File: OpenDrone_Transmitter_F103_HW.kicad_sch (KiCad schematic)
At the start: 75 parts, among them J1 Conn_01x03, J10 Conn_01x04, J11 Conn_01x03, J12 Conn_01x04, J13 Conn_01x02, J14 Conn_01x05, J15 Conn_01x02, J16 Conn_02x04_Odd_Even, J17 Conn_01x02, J18 Conn_01x02, J19 Conn_01x03, J2 Conn_01x05, J20 Conn_01x02, J21 Conn_01x02, J22 Conn_01x02, J3 Conn_01x03, J4 Conn_01x03, J5 Conn_01x03, J6 Conn_01x02, J7 Conn_01x02, J8 Conn_01x03, J9 Conn_01x03, SW1 RESET, U1 STM32F103C8Tx, U2 AMS1117-3.3, U3 TPS54331, Y2 Crystal_GND24

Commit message: update project
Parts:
- added D4: SS24, Diode_SMD:D_SMA, symbol Device:D_Small
- J10, J12: footprint Footprint:Connector_XH_1x04_P1.25mm_Horizontal -> Footprint:Connector_XH_1x04_P1.25mm_Vertical
- J14, J2: footprint Footprint:Connector_XH_1x05_P1.25mm_Horizontal -> Footprint:Connector_XH_1x05_P1.25mm_Vertical
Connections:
- net GND: now also D4.2 (A)
- net VBAT: now also D4.1 (K)
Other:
- moved on the sheet: C1, C11, C12, C13, C14, C2, C20, C4, C5, D1, D2, D3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

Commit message: update project
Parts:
- R1: value TBD -> 10k
- R2: value TBD -> 3,3k
- R6: value TBD -> 0R
- U3: footprint Package_SO:SOIC-8-1EP_3.9x4.9mm_P1.27mm_EP2.29x3mm_ThermalVias -> Package_SO:SOIC-8-1EP_3.9x4.9mm_P1.27mm_EP2.29x3mm
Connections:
- net +3V3: now also J3.1 (Pin_1)
- net GND: now also J3.3 (Pin_3)
- net LEFT_JOYSTICK_IN1: now also J3.2 (Pin_2)
- net at R2.1, R6.2: now also U3.5 (VSENSE)
- net at R1.2, R6.1: no longer U3.5 (VSENSE)
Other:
- moved on the sheet: R6
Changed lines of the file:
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@@
 	)
 	(junction
+		(at 110.49 184.15)
+		(diameter 0)
+		(color 0 0 0 0)
+	)
+	(junction
 		(at 110.49 190.5)
 		(diameter 0)
@@
 	)
 	(junction
-		(at 110.49 180.34)
-		(diameter 0)
-		(color 0 0 0 0)
-	)
-	(junction
 		(at 38.1 172.72)
 		(diameter 0)
@@
 	(wire
 		(pts
+			(xy 82.55 180.34) (xy 105.41 180.34)
+		)
+		(stroke
+			(width 0)
+			(type default)
+		)
+	)
+	(wire
+		(pts
 			(xy 127 180.34) (xy 127 190.5)
 		)
@@
 	(wire
 		(pts
-			(xy 110.49 180.34) (xy 110.49 179.07)
-		)
-		(stroke
-			(width 0)
-			(type default)
-		)
-	)
-	(wire
-		(pts
 			(xy 138.43 34.29) (xy 143.51 34.29)
 		)
@@
 	(wire
 		(pts
-			(xy 82.55 180.34) (xy 110.49 180.34)
+			(xy 105.41 184.15) (xy 110.49 184.15)
 		)
 		(stroke
@@
 	(wire
 		(pts
+			(xy 110.49 184.15) (xy 110.49 185.42)
+		)
+		(stroke
+			(width 0)
+			(type default)
+		)
+	)
+	(wire
+		(pts
 			(xy 113.03 104.14) (xy 124.46 104.14)
 		)
@@
 	(wire
 		(pts
+			(xy 105.41 180.34) (xy 105.41 184.15)
+		)
+		(stroke
+			(width 0)
+			(type default)
+		)
+	)
+	(wire
+		(pts
 			(xy 133.35 170.18) (xy 135.89 170.18)
 		)
@@
 	(global_label "LEFT_JOYSTICK_IN1"
 		(shape input)
-		(at 189.23 31.75 0)
+		(at 190.5 31.75 0)
 		(fields_autoplaced yes)
 		(effects
@@
 		)
 		(property "Intersheetrefs" "${INTERSHEET_REFS}"
-			(at 210.2371 31.75 0)
+			(at 211.5071 31.75 0)
 			(effects
 				(font
@@
 			)
 		)
-		(property "Value" "TBD"
+		(property "Value" "3,3k"
 			(at 112.268 188.722 0)
 			(effects
@@
 			)
 		)
-		(property "Footprint" "Package_SO:SOIC-8-1EP_3.9x4.9mm_P1.27mm_EP2.29x3mm_ThermalVias"
+		(property "Footprint" "Package_SO:SOIC-8-1EP_3.9x4.9mm_P1.27mm_EP2.29x3mm"
 			(at 69.85 177.8 0)
 			(effects
@@
 	(symbol
 		(lib_id "power:GND")
-		(at 189.23 34.29 90)
+		(at 190.5 34.29 90)
 		(unit 1)
 		(exclude_from_sim no)
@@
 		(fields_autoplaced yes)
 		(property "Reference" "#PWR025"
-			(at 195.58 34.29 0)
+			(at 196.85 34.29 0)
 			(effects
 				(font
@@
 		)
 		(property "Value" "GND"
-			(at 193.04 34.2899 90)
+			(at 194.31 34.2899 90)
 			(effects
 				(font
@@
 		)
 		(property "Footprint" ""
-			(at 189.23 34.29 0)
+			(at 190.5 34.29 0)
 			(effects
 				(font
@@
 		)
 		(property "Datasheet" ""
-			(at 189.23 34.29 0)
+			(at 190.5 34.29 0)
 			(effects
 				(font
@@
 		)
 		(property "Description" "Power symbol creates a global label with name \"GND\" , ground"
-			(at 189.23 34.29 0)
+			(at 190.5 34.29 0)
 			(effects
 				(font
@@
 	(symbol
 		(lib_id "power:+3V3")
-		(at 189.23 29.21 270)
+		(at 190.5 29.21 270)
 		(unit 1)
 		(exclude_from_sim no)
@@
 		(fields_autoplaced yes)
 		(property "Reference" "#PWR026"
-			(at 185.42 29.21 0)
+			(at 186.69 29.21 0)
 			(effects
 				(font
@@
 		)
 		(property "Value" "+3V3"
-			(at 193.04 29.2099 90)
+			(at 194.31 29.2099 90)
 			(effects
 				(font
@@
 		)
 		(property "Footprint" ""
-			(at 189.23 29.21 0)
+			(at 190.5 29.21 0)
 			(effects
 				(font
@@
 		)
 		(property "Datasheet" ""
-			(at 189.23 29.21 0)
+			(at 190.5 29.21 0)
 			(effects
 				(font
@@
 		)
 		(property "Description" "Power symbol creates a global label with name \"+3V3\""
-			(at 189.23 29.21 0)
+			(at 190.5 29.21 0)
 			(effects
 				(font
@@
 			)
 		)
-		(property "Value" "TBD"
+		(property "Value" "10k"
 			(at 112.268 177.8 0)
 			(effects
@@
 	(symbol
 		(lib_id "Device:R_Small")
-		(at 110.49 182.88 0)
+		(at 110.49 181.61 0)
 		(unit 1)
 		(exclude_from_sim no)
@@
 		(dnp no)
 		(property "Reference" "R6"
-			(at 112.268 181.61 0)
+			(at 112.268 180.34 0)
 			(effects
 				(font
@@
 			)
 		)
-		(property "Value" "TBD"
-			(at 112.268 183.642 0)
+		(property "Value" "0R"
+			(at 112.268 182.372 0)
 			(effects
 				(font
@@
 		)
 		(property "Footprint" "Resistor_SMD:R_0603_1608Metric"
-			(at 110.49 182.88 0)
+			(at 110.49 181.61 0)
 			(effects
 				(font
@@
 		)
 		(property "Datasheet" "~"
-			(at 110.49 182.88 0)
+			(at 110.49 181.61 0)
 			(effects
 				(font
@@
 		)
 		(property "Description" "Resistor, small symbol"
-			(at 110.49 182.88 0)
+			(at 110.49 181.61 0)
 			(effects
 				(font

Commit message: complete v1.0
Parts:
- added D5: D_Small, LED_SMD:LED_0603_1608Metric, symbol Device:D_Small
- added R17: 330R, Resistor_SMD:R_0603_1608Metric, symbol Device:R_Small
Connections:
- net +3V3: now also J16.1 (Pin_1), R17.2; no longer J16.2 (Pin_2)
- net BUTTON1: now also J14.4 (Pin_4), U1.30 (PA9); no longer J14.1 (Pin_1), U1.22 (PB11)
- net BUTTON2: now also J14.3 (Pin_3); no longer J14.2 (Pin_2)
- net BUTTON3: now also J14.2 (Pin_2); no longer J14.3 (Pin_3)
- net BUTTON4: now also J14.1 (Pin_1); no longer J14.4 (Pin_4)
- net GND: now also J16.2 (Pin_2), D5.1 (K); no longer J16.1 (Pin_1)
- net NRF24_CE: now also J16.4 (Pin_4); no longer J16.3 (Pin_3)
- net NRF24_CLK: now also J16.6 (Pin_6); no longer J16.5 (Pin_5)
- net NRF24_CS: now also J16.3 (Pin_3); no longer J16.4 (Pin_4)
- net NRF24_IRQ: now also J16.7 (Pin_7), U1.22 (PB11); no longer J16.8 (Pin_8), U1.30 (PA9)
- net NRF24_MISO: now also J16.8 (Pin_8); no longer J16.7 (Pin_7)
- net NRF24_MOSI: now also J16.5 (Pin_5); no longer J16.6 (Pin_6)
- net STM32_CLK: now also J2.4 (Pin_4); no longer J2.3 (Pin_3)
- net STM32_DIO: now also J2.3 (Pin_3); no longer J2.4 (Pin_4)
- net ADC_RESERVED: no longer names the net of U1.19 (PB1)
- new net: D5.2 (A), R17.1
- no-connect marks 1 -> 9
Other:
- moved on the sheet: C15, C27, C28, C29, J12, J13, J15, J17, J18, J20, J21, J22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

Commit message: update
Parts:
- added C10, C21, C30, C31: 100nF, KiCad-Lib:C_0603_1608Metric, symbol Device:C_Small
- added J23: Conn_01x08, KiCad-Lib:Connector_ZH_1x08_P1.25mm_Vertical, symbol Connector_Generic:Conn_01x08
- added R18, R19, R20, R21: 1k, KiCad-Lib:R_0603_1608Metric, symbol Device:R_Small
- C1, C2, C20, C4, C5, C9: footprint Capacitor_SMD:C_1210_3225Metric -> KiCad-Lib:C_1210_3225Metric
- C11, C12, C13, C14, C15, C16, C17, C18, C19, C22, C23, C24, C25, C26, C27, C28, C29, C3, C6, C7, C8: footprint Capacitor_SMD:C_0603_1608Metric -> KiCad-Lib:C_0603_1608Metric
- D1, D2, D3, D4: footprint Diode_SMD:D_SMA -> KiCad-Lib:D_SMA
- D5: footprint LED_SMD:LED_0603_1608Metric -> KiCad-Lib:LED_0603_1608Metric
- J1, J11, J19, J3, J4, J5, J8, J9: footprint Footprint:Connector_XH_1x03_P1.25mm_Vertical -> KiCad-Lib:Connector_ZH_1x03_P1.25mm_Vertical
- J10, J12: footprint Footprint:Connector_XH_1x04_P1.25mm_Vertical -> KiCad-Lib:Connector_ZH_1x04_P1.25mm_Vertical
- J13, J15, J17, J18, J20, J21, J22, J6: footprint Footprint:Connector_XH_1x02_P1.25mm_Vertical -> KiCad-Lib:Connector_ZH_1x02_P1.25mm_Vertical
- J14, J2: footprint Footprint:Connector_XH_1x05_P1.25mm_Vertical -> KiCad-Lib:Connector_ZH_1x05_P1.25mm_Vertical
- J7: footprint Connector_JST:JST_EH_B2B-EH-A_1x02_P2.50mm_Vertical -> KiCad-Lib:Connector_ZH_1x02_P1.25mm_Vertical
- L1: footprint Footprint:Inductor_SMD_4D28 -> KiCad-Lib:Inductor_SMD_4D28
- R1, R10, R11, R12, R13, R14, R15, R16, R17, R2, R3, R4, R5, R6, R7, R8, R9: footprint Resistor_SMD:R_0603_1608Metric -> KiCad-Lib:R_0603_1608Metric
- SW1: footprint Footprint:Button_SMD_4.2x3.3x2.5mm -> KiCad-Lib:Button_SMD_4.2x3.3x2.5mm
- U3: footprint Package_SO:SOIC-8-1EP_3.9x4.9mm_P1.27mm_EP2.29x3mm -> KiCad-Lib:SOIC-8-1EP_3.9x4.9mm_P1.27mm_EP2.29x3mm
- U4: footprint Footprint:Board -> Proj-Lib:Board
- Y2: footprint Crystal:Crystal_SMD_3225-4Pin_3.2x2.5mm -> KiCad-Lib:Crystal_SMD_3225-4Pin_3.2x2.5mm
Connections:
- net +3V3: now also J23.8 (Pin_8), R18.1, R19.1, R20.1, R21.1
- net BUTTON1: now also J14.1 (Pin_1); no longer J14.4 (Pin_4)
- net BUTTON2: now also J14.2 (Pin_2); no longer J14.3 (Pin_3)
- net BUTTON3: now also J14.3 (Pin_3); no longer J14.2 (Pin_2)
- net BUTTON4: now also J14.4 (Pin_4); no longer J14.1 (Pin_1)
- net GND: now also J1.2 (Pin_2), J11.2 (Pin_2), J19.2 (Pin_2), J20.2 (Pin_2), J21.2 (Pin_2), J22.2 (Pin_2), J3.2 (Pin_2), J4.2 (Pin_2), J5.2 (Pin_2), J6.2 (Pin_2), J8.2 (Pin_2), J9.2 (Pin_2), C10.2, C21.2, C30.2, C31.2, J23.7 (Pin_7); no longer J1.3 (Pin_3), J11.3 (Pin_3), J19.3 (Pin_3), J3.3 (Pin_3), J4.3 (Pin_3), J5.3 (Pin_3), J8.3 (Pin_3), J9.3 (Pin_3)
- net I2C1_SCL: now also J10.3 (Pin_3); no longer J10.4 (Pin_4)
- net I2C1_SDA: now also J10.4 (Pin_4); no longer J10.3 (Pin_3)
- net LEFT_JOYSTICK_IN1: now also J3.3 (Pin_3); no longer J3.2 (Pin_2)
- net LEFT_JOYSTICK_IN2: now also J4.3 (Pin_3); no longer J4.2 (Pin_2)
- net NRF24_CE: now also J23.5 (Pin_5)
- net NRF24_CLK: now also J23.3 (Pin_3)
- net NRF24_CS: now also U1.22 (PB11), J23.6 (Pin_6); no longer U1.25 (PB12)
- net NRF24_IRQ: now also U1.38 (PA15), J23.2 (Pin_2); no longer U1.22 (PB11)
- net NRF24_MISO: now also J23.1 (Pin_1)
- net NRF24_MOSI: now also J23.4 (Pin_4)
- net RIGHT_JOYSTICK_IN1: now also J19.3 (Pin_3); no longer J19.2 (Pin_2)
- net RIGHT_JOYSTICK_IN2: now also J5.3 (Pin_3); no longer J5.2 (Pin_2)
- net UART1_RX: now also J12.4 (Pin_4); no longer J12.3 (Pin_3)
- net UART1_TX: now also J12.3 (Pin_3); no longer J12.4 (Pin_4)
- net VOLUME_1: now also J8.3 (Pin_3); no longer J8.2 (Pin_2)
- net VOLUME_2: now also J1.3 (Pin_3); no longer J1.2 (Pin_2)
- net VOLUME_3: now also J9.3 (Pin_3); no longer J9.2 (Pin_2)
- net VOLUME_4: now also J11.3 (Pin_3); no longer J11.2 (Pin_2)
- net PC13: now reaches J22.1 (Pin_1)
- net PC13: now also U1.2 (PC13), C31.1, R21.2
- net PB3: now reaches J21.1 (Pin_1)
- net PB3: now also U1.39 (PB3), C21.1, R19.2
- net PB12: now reaches J6.1 (Pin_1)
- net PB12: now also U1.25 (PB12), C10.1, R18.2
- net PB1: now reaches J20.1 (Pin_1)
- net PB1: now also U1.19 (PB1), C30.1, R20.2
- net SWITCH1 renamed PB2
- net SWITCH2 renamed PB4
- net SWITCH3 renamed PB10
- net SWITCH4 renamed PB5
- no-connect marks 9 -> 1
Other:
- moved on the sheet: J20, J21, J22, J6

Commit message: update schematic
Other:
- note removed: "CONNECTOR"
- moved on the sheet: C1, C10, C11, C12, C13, C14, C15, C2, C20, C21, C22, C23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

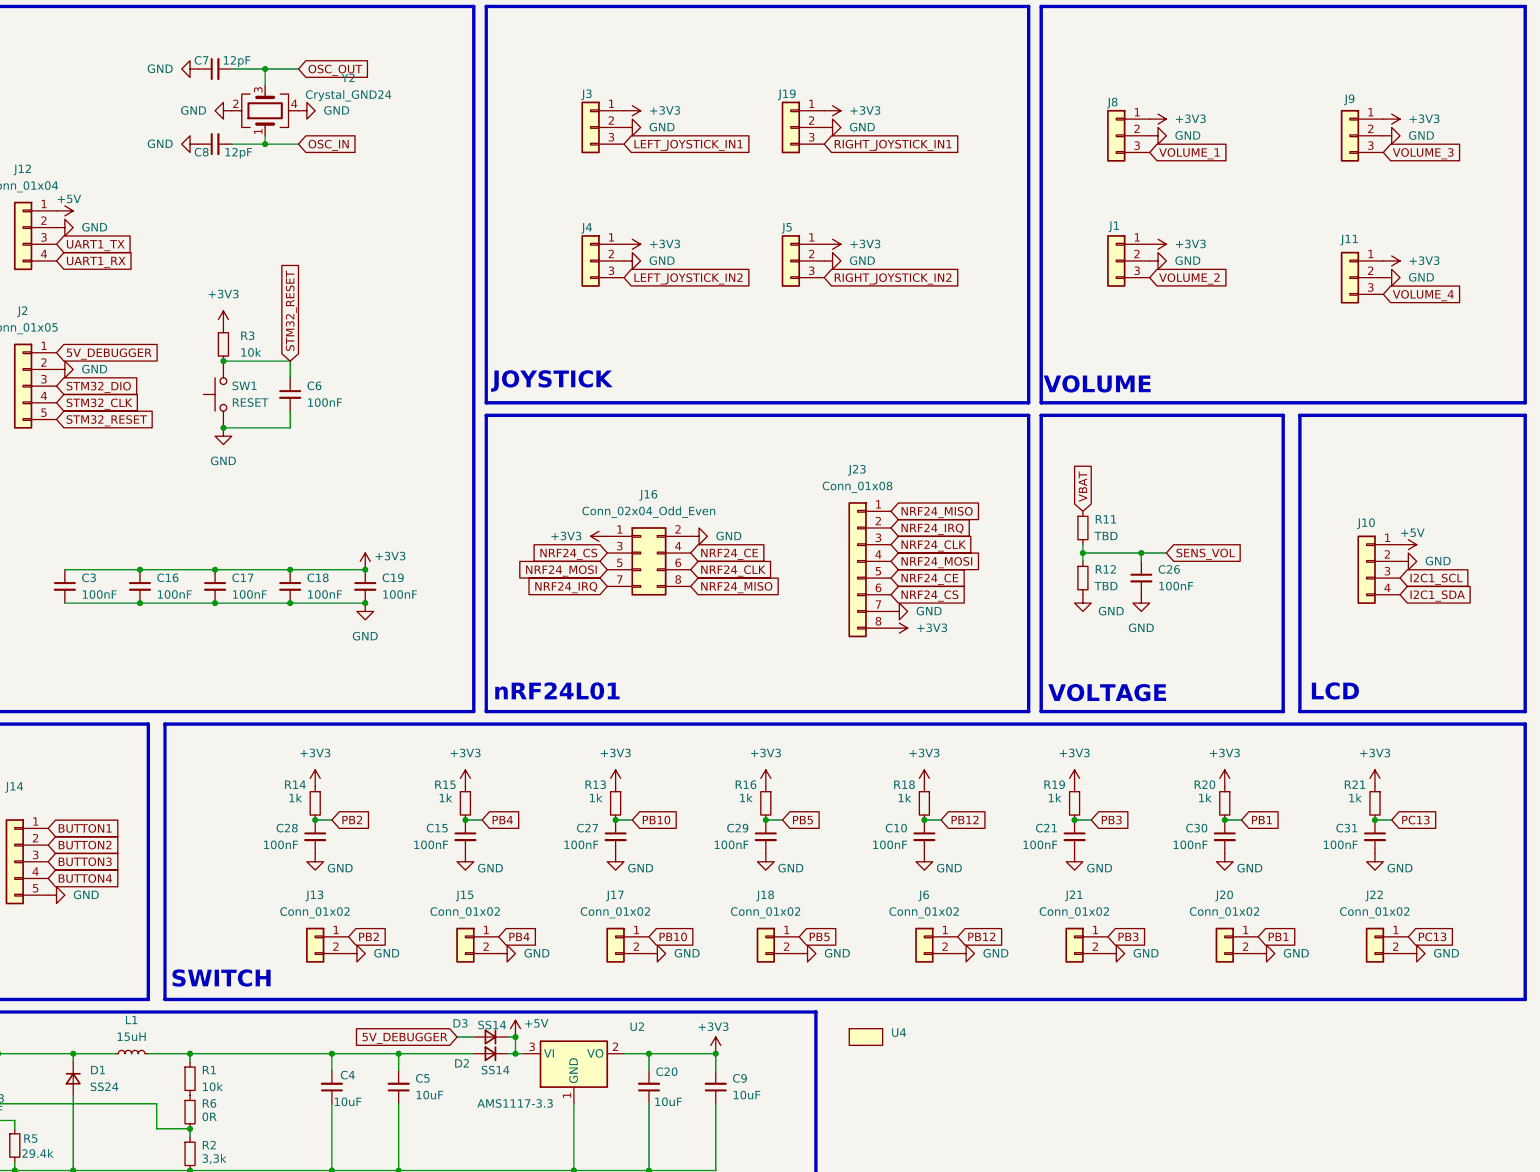
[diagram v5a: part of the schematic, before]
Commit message: change pin order in joystick
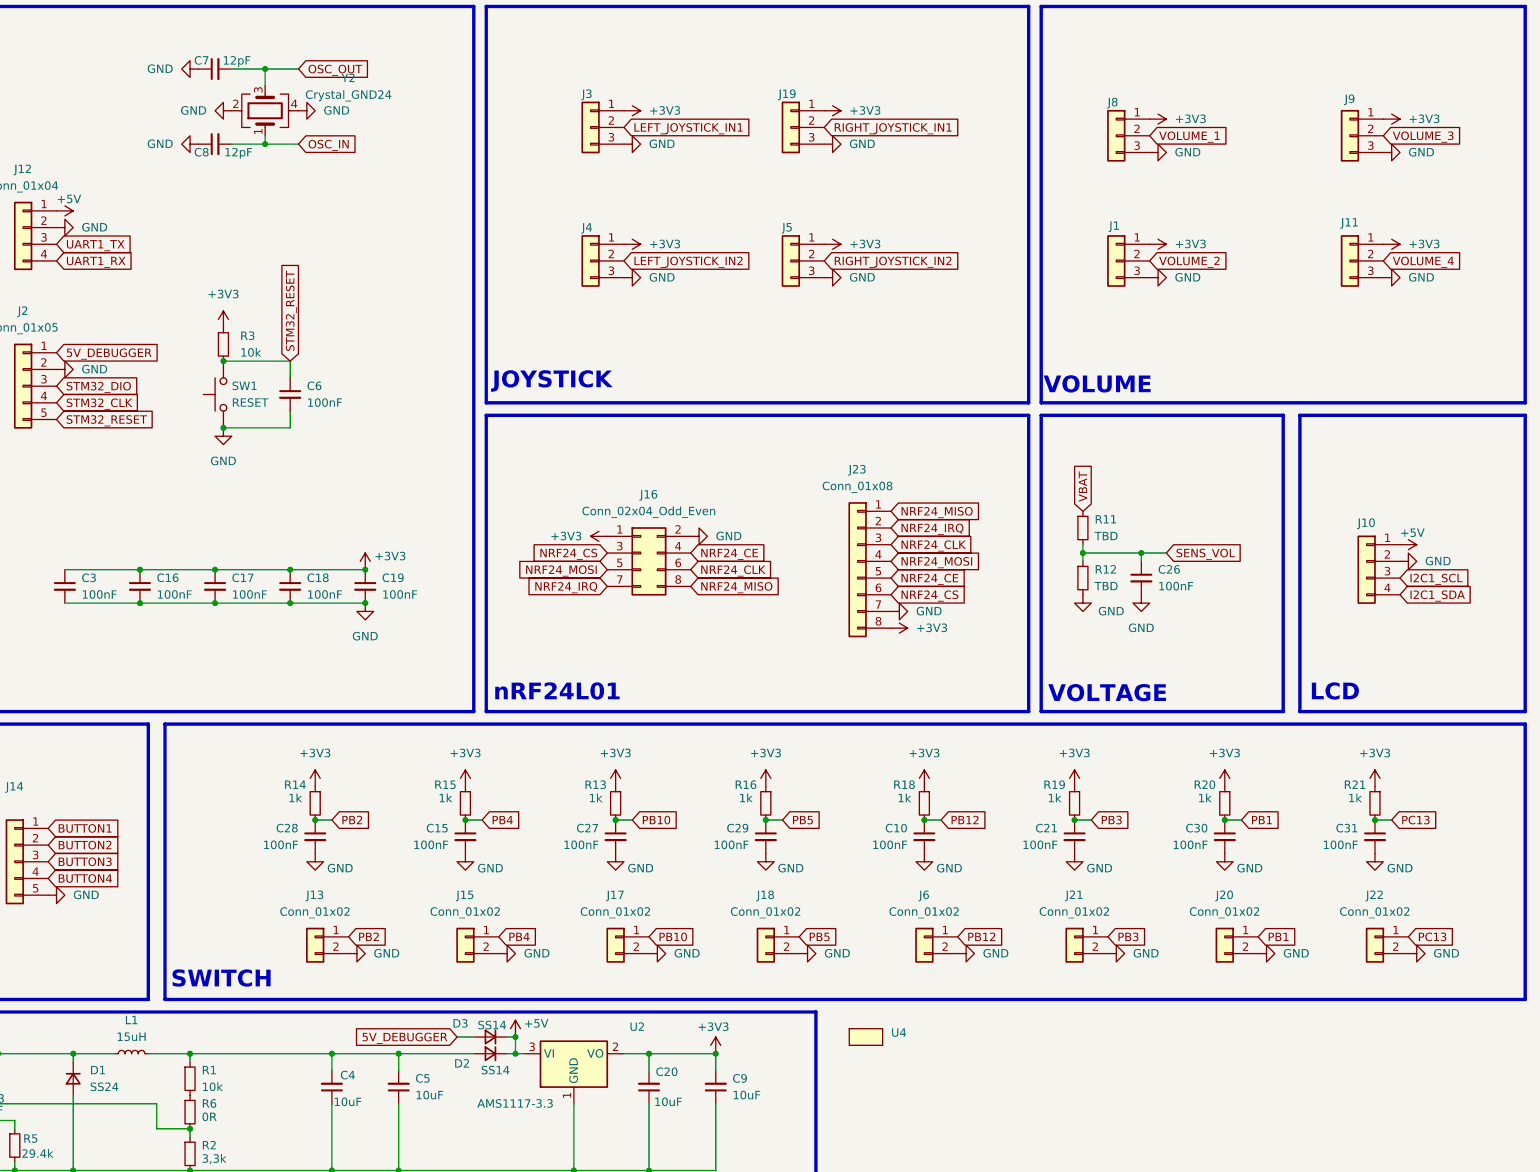
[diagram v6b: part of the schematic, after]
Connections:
- net GND: now also J1.3 (Pin_3), J11.3 (Pin_3), J19.3 (Pin_3), J3.3 (Pin_3), J4.3 (Pin_3), J5.3 (Pin_3), J8.3 (Pin_3), J9.3 (Pin_3); no longer J1.2 (Pin_2), J11.2 (Pin_2), J19.2 (Pin_2), J3.2 (Pin_2), J4.2 (Pin_2), J5.2 (Pin_2), J8.2 (Pin_2), J9.2 (Pin_2)
- net LEFT_JOYSTICK_IN1: now also J3.2 (Pin_2); no longer J3.3 (Pin_3)
- net LEFT_JOYSTICK_IN2: now also J4.2 (Pin_2); no longer J4.3 (Pin_3)
- net RIGHT_JOYSTICK_IN1: now also J19.2 (Pin_2); no longer J19.3 (Pin_3)
- net RIGHT_JOYSTICK_IN2: now also J5.2 (Pin_2); no longer J5.3 (Pin_3)
- net VOLUME_1: now also J8.2 (Pin_2); no longer J8.3 (Pin_3)
- net VOLUME_2: now also J1.2 (Pin_2); no longer J1.3 (Pin_3)
- net VOLUME_3: now also J9.2 (Pin_2); no longer J9.3 (Pin_3)
- net VOLUME_4: now also J11.2 (Pin_2); no longer J11.3 (Pin_3)
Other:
- moved on the sheet: J11
